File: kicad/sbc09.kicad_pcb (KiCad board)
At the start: 4 copper layers, 160 x 99.1 mm, 72 parts, among them J1 Conn_01x03_Male, J2 Conn_01x06_Male, J3 Conn_01x06_Male, J4 Conn_01x06_Male, J5 DB9_Female_MountingHoles, J6 Conn_02x25_Odd_Even, Q1 2N7000, SW1 SW_Push, U1 74LS245, U10 74LS670, U11 74LS670, U12 AS6C4008-55PCN, U13 SST39SF040-DIP, U14 SST39SF040-DIP, U15 XR68C681CJ, U16 MAX232, U2 74LS245, U3 74LS245, U4 ATF22V10C, U5 ATF22V10C, U6 MC6809E, U7 74HCT125, U8 74LS670, U9 74LS670, X1 8MHz, X2 3.6864MHz

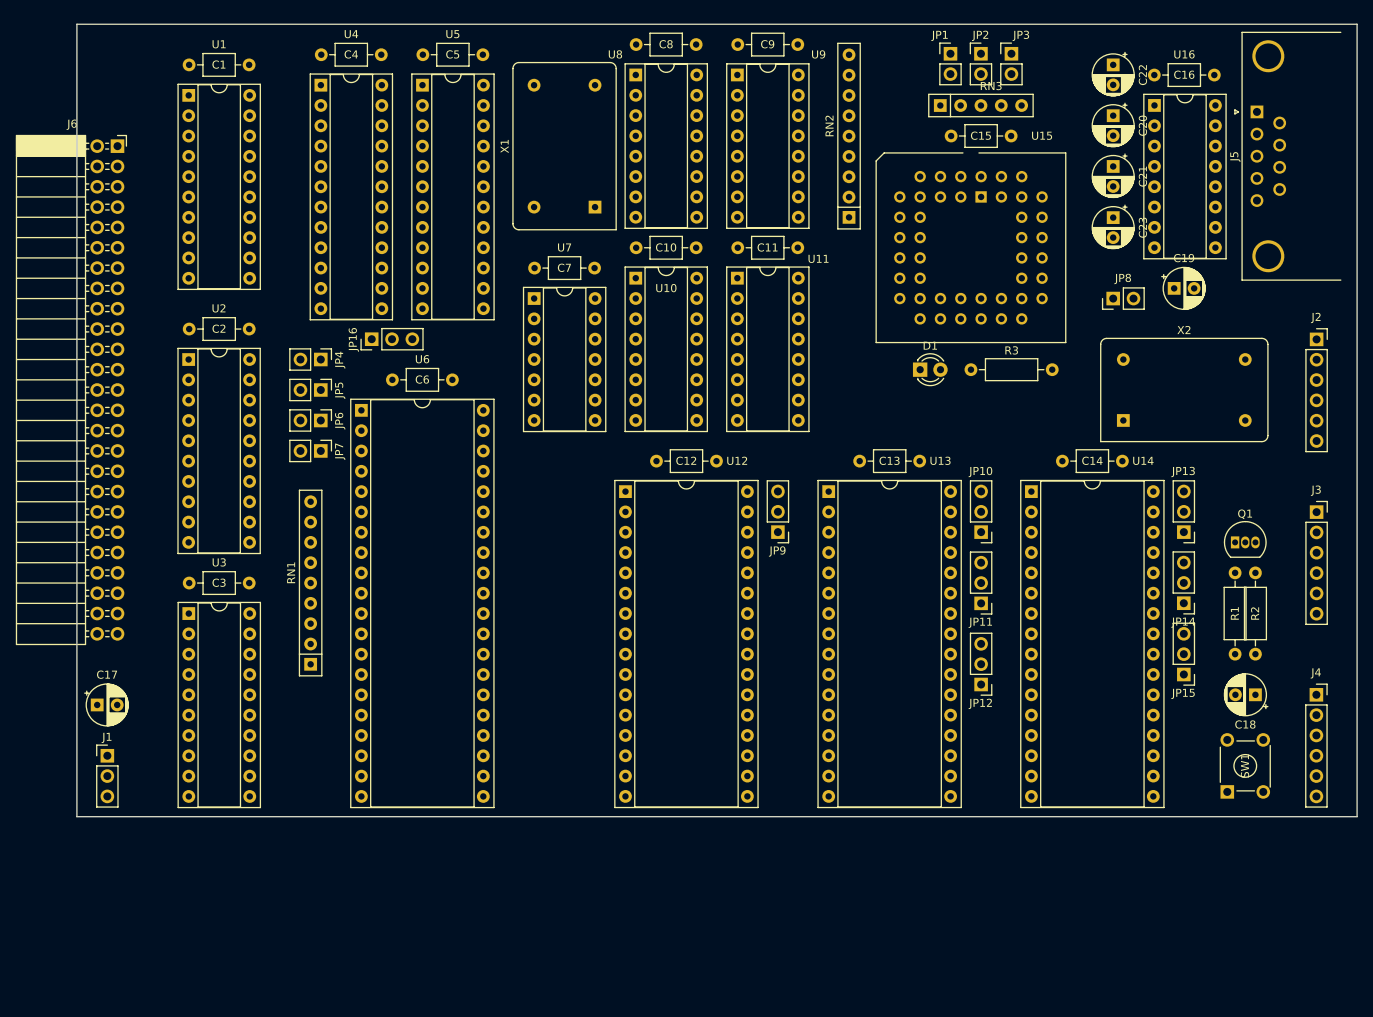
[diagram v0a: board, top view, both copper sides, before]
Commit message: Started manually routing the board
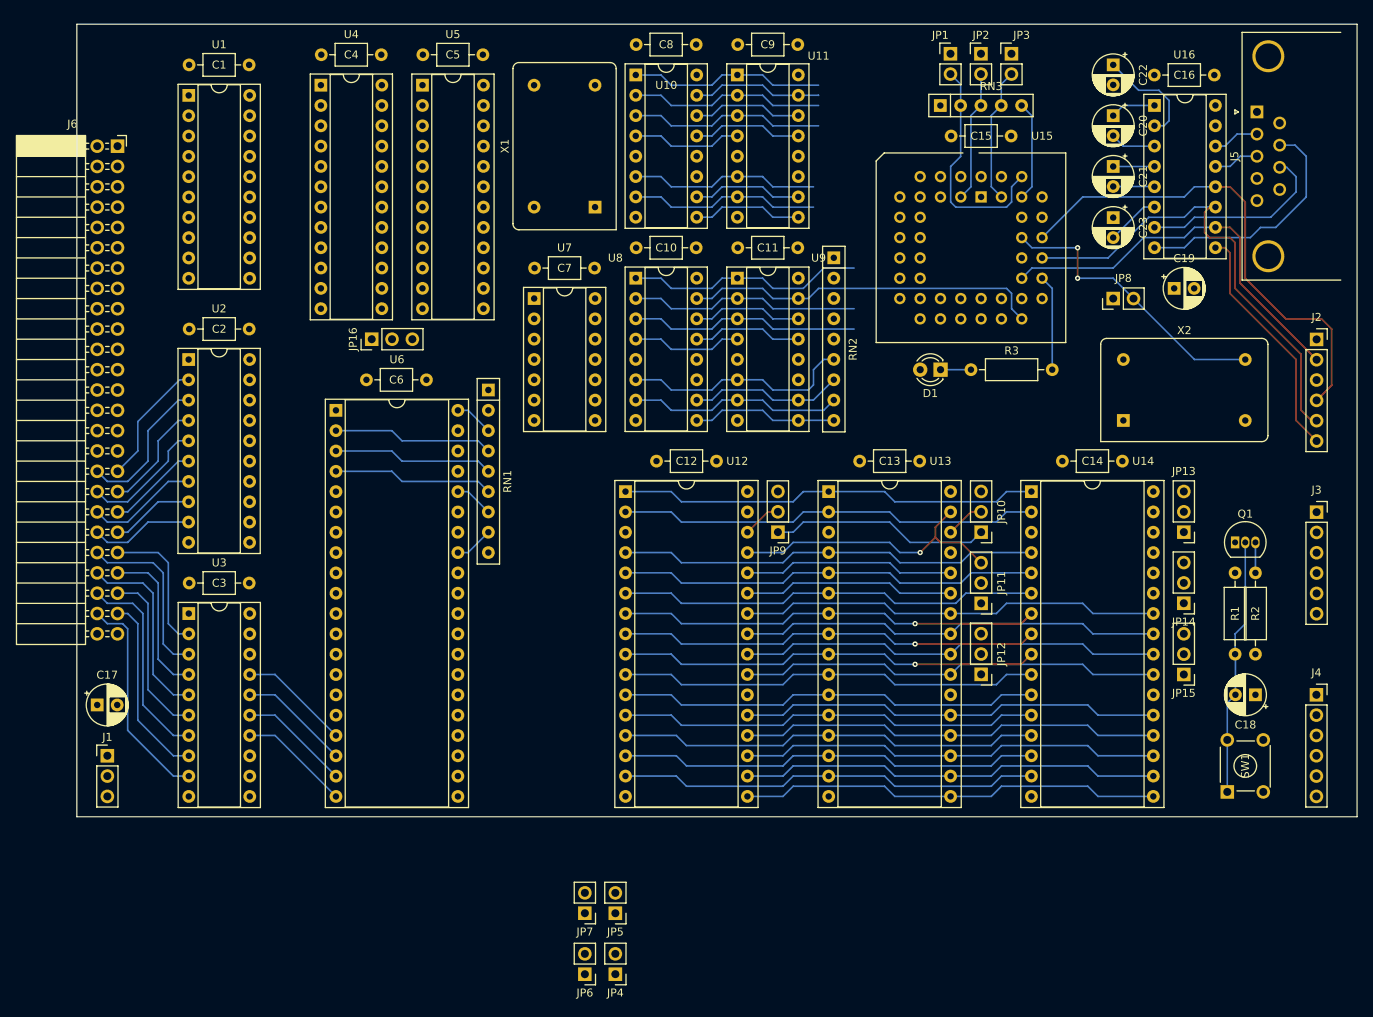
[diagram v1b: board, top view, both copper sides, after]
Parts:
- moved JP4 85.2 mm to (146.1, 169.5), turned to 180 degrees
- moved JP6 76.7 mm to (142.2, 169.5), turned to 180 degrees
- moved JP5 75.1 mm to (146.1, 161.9), turned to 180 degrees
- moved JP7 66.5 mm to (142.2, 161.9), turned to 180 degrees
- moved RN1 40.9 mm to (130.2, 96.5), turned to -90 degrees
- moved U10 25.4 mm to (148.6, 57.1)
- moved U11 25.4 mm to (161.3, 57.1)
- moved U8 25.4 mm to (148.6, 82.5)
- moved U9 25.4 mm to (161.3, 82.5)
- moved RN2 5.40 mm to (173.4, 80.0), turned to -90 degrees
- moved C6 3.25 mm to (114.9, 95.2)
- moved U6 3.18 mm to (111.1, 99.1)
- moved D1 2.54 mm to (186.7, 94.0), turned to 180 degrees
- moved JP12 1.27 mm to (191.8, 132.1)
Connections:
- JP5 pad 2: Net-(JP5-Pad2) -> Net-(RN1-Pad2)
- RN1 pad 2: nNMI -> Net-(RN1-Pad2)
- RN1 pad 3: nIRQ -> nHALT
- RN1 pad 4: nFIRQ -> nNMI
- RN1 pad 5: nHALT -> nIRQ
- RN1 pad 6: BUSY_BREQ -> nFIRQ
- RN1 pad 8: Net-(JP5-Pad2) -> BUSY_BREQ
- RN2 pad 7: /QA16 -> /QA14
- RN2 pad 8: /QA15 -> /QA16
- RN2 pad 9: /QA14 -> /QA15
- U7 pad 1: Net-(JP5-Pad2) -> Net-(RN1-Pad2)
- U7 pad 4: Net-(JP5-Pad2) -> Net-(RN1-Pad2)
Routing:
- net /D0: track 0.00 -> 97.7 mm
- net /D1: track 0.00 -> 82.8 mm
- net /D2: track 0.00 -> 81.7 mm
- net /D3: track 0.00 -> 81.7 mm
- net /A0: track 0.00 -> 80.3 mm
- net /A1: track 0.00 -> 80.3 mm
- net /QA16: track 0.00 -> 79.7 mm
- net /D7: track 0.00 -> 77.3 mm
- net /D5: track 0.00 -> 77.3 mm
- net /D6: track 0.00 -> 77.3 mm
- net /D4: track 0.00 -> 69.1 mm
- net /A10: track 0.00 -> 66.8 mm
- net /A12: track 0.00 -> 66.8 mm
- net /A9: track 0.00 -> 66.8 mm
- net /A11: track 0.00 -> 66.8 mm
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- added copper zone on In2.Cu, net VCC
- removed copper zone on In2.Cu, net (none)

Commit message: Started manually routing the board
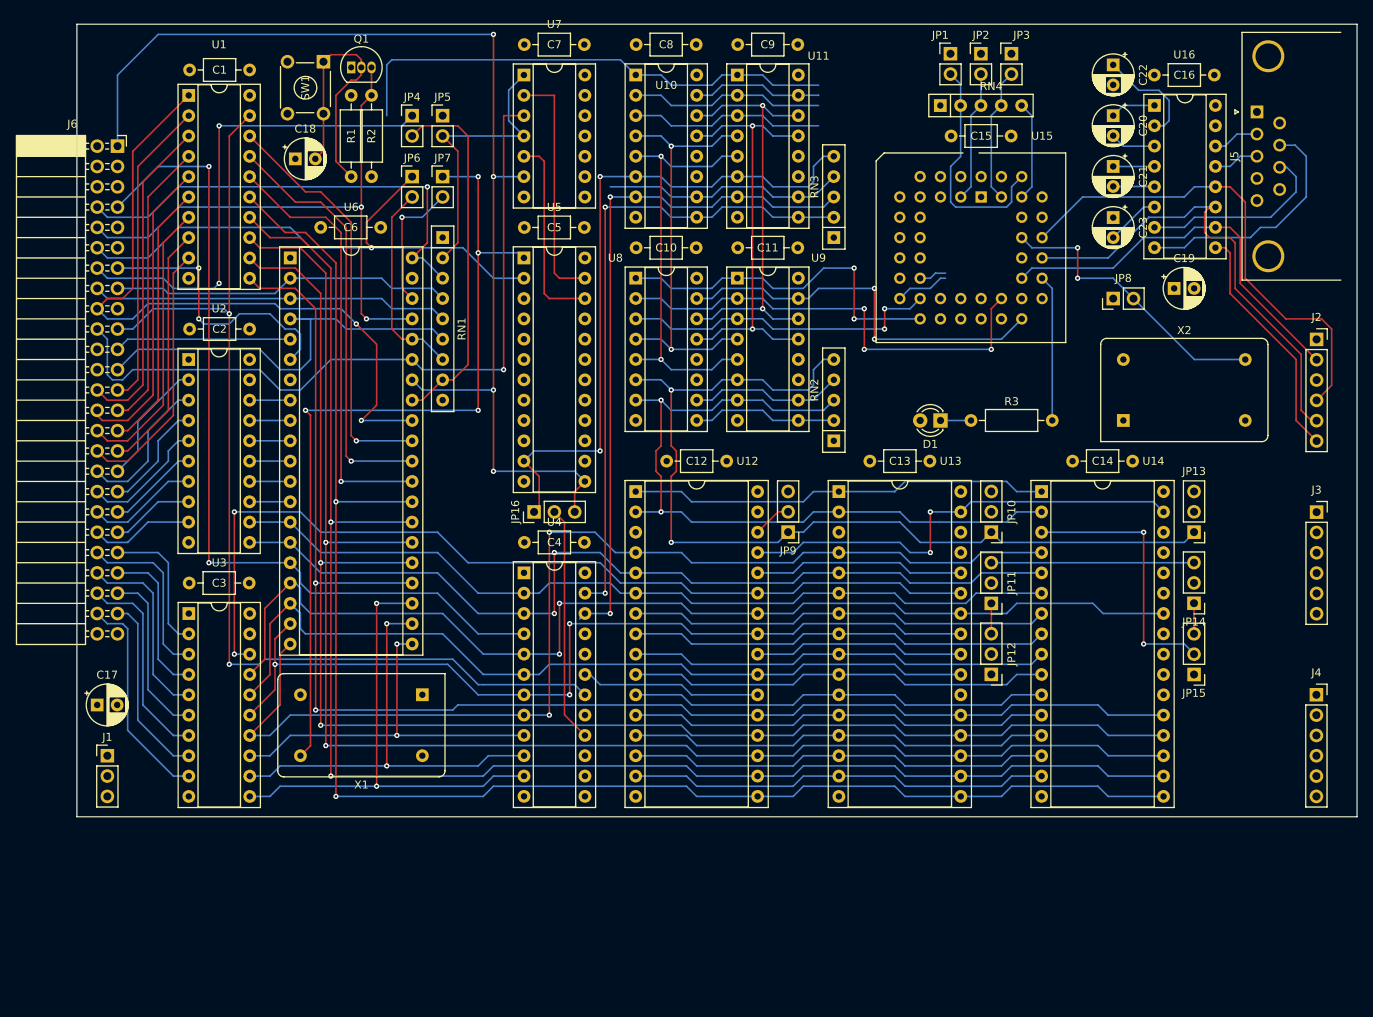
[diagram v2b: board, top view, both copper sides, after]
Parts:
- added RN3: 10K, Resistor_THT:R_Array_SIP5, F.Cu at (173.4, 77.5)
- RN2: footprint Resistor_THT:R_Array_SIP9 -> Resistor_THT:R_Array_SIP5
- moved SW1 145.2 mm to (109.6, 55.5), turned to -90 degrees
- moved C18 137.4 mm to (106.0, 67.6), turned to 0 degrees
- moved R1 125.6 mm to (113.0, 69.8)
- moved R2 125.6 mm to (115.6, 69.8)
- moved Q1 125.4 mm to (113.0, 56.2)
- moved JP4 110.3 mm to (120.7, 62.2), turned to 0 degrees
- moved JP5 102.0 mm to (124.5, 62.2), turned to 0 degrees
- moved JP6 102.0 mm to (120.7, 69.8), turned to 0 degrees
- moved JP7 93.8 mm to (124.5, 69.8), turned to 0 degrees
- moved U4 66.0 mm to (134.6, 119.4)
- moved C4 66.0 mm to (134.7, 115.6)
- moved X1 64.7 mm to (121.9, 134.6), turned to 180 degrees
- moved JP16 29.6 mm to (135.9, 111.8)
- moved C7 28.0 mm to (134.7, 53.3)
- moved U7 28.0 mm to (134.6, 57.1)
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- renumbered RN3 to RN4
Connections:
- RN2 pad 2: QA21 -> /QA15
- RN2 pad 3: QA20 -> /QA16
- RN2 pad 4: QA19 -> /QA14
- RN2 pad 5: /QA18 -> /QA17
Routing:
- net /D5: track 77.3 -> 251.5 mm, vias 0 -> 2
- net /D3: track 81.7 -> 237.2 mm, vias 0 -> 4
- net E: track 0.00 -> 143.4 mm, vias 0 -> 4
- net /D4: track 69.1 -> 210.0 mm, vias 0 -> 3
- net nCSEXT: track 0.00 -> 131.5 mm, vias 0 -> 2
- net /D6: track 77.3 -> 208.5 mm, vias 0 -> 2
- net /D7: track 77.3 -> 205.4 mm, vias 0 -> 2
- net /A14: track 0.00 -> 109.2 mm, vias 0 -> 4
- net A8: track 0.00 -> 106.9 mm, vias 0 -> 2
- net CLKX4: track 0.00 -> 105.2 mm, vias 0 -> 4
- net Q: track 0.00 -> 94.0 mm, vias 0 -> 1
- net /A8X: track 26.5 -> 115.8 mm, vias 0 -> 2
- net /A15: track 27.5 -> 115.6 mm, vias 0 -> 4
- net RnW: track 0.00 -> 87.5 mm, vias 0 -> 2
- net /D2: track 81.7 -> 165.1 mm, vias 0 -> 4
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
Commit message: Started manually routing the board
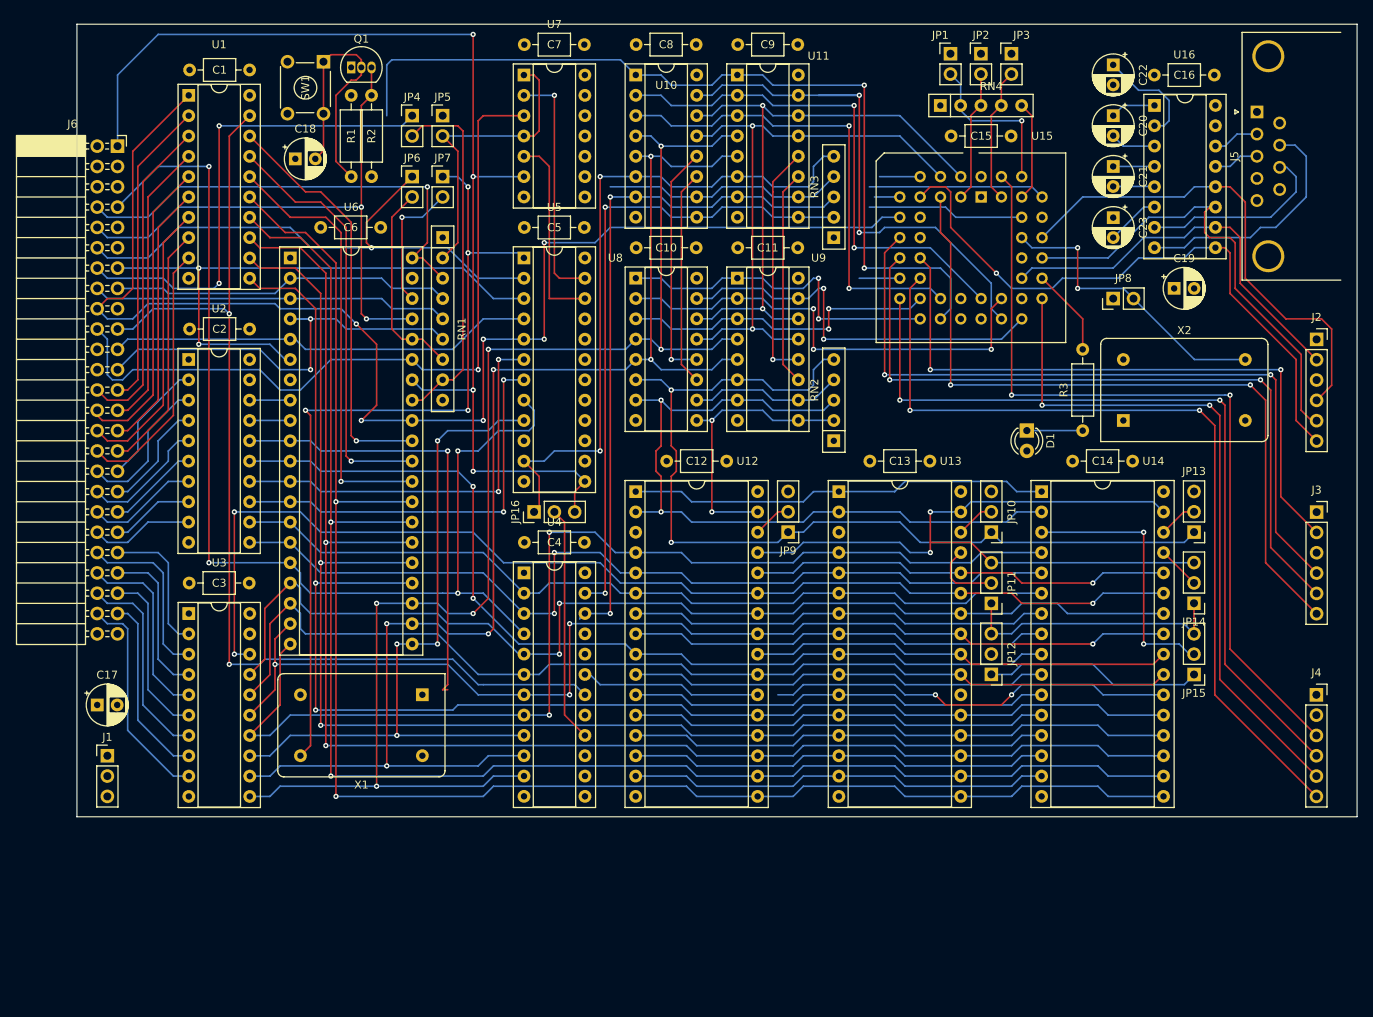
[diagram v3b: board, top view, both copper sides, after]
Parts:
- moved R3 14.0 mm to (204.5, 101.6), turned to 90 degrees
- moved D1 10.9 mm to (197.5, 101.6), turned to -90 degrees
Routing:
- net /SDCS: track 3.44 -> 107.5 mm, vias 0 -> 2
- net /SDMISO: track 0.00 -> 102.2 mm, vias 0 -> 2
- net /SDMOSI: track 6.77 -> 102.2 mm, vias 0 -> 2
- net /CTSB: track 0.00 -> 93.5 mm, vias 0 -> 2
- net /RXDB: track 0.00 -> 93.4 mm, vias 0 -> 2
- net /TXDB: track 0.00 -> 91.7 mm, vias 0 -> 2
- net /SDCLK: track 0.00 -> 86.2 mm, vias 0 -> 2
- net RnW: track 87.5 -> 172.0 mm, vias 2 -> 6
- net /RTSB: track 0.00 -> 80.5 mm, vias 0 -> 2
- net /A3: track 57.9 -> 122.5 mm, vias 0 -> 2
- net /A14: track 109.2 -> 170.9 mm, vias 4 -> 6
- net /A15: track 115.6 -> 176.5 mm, vias 4 -> 6
- net /A2: track 57.9 -> 114.0 mm, vias 0 -> 1
- net /D4: track 210.0 -> 261.9 mm, vias 3 -> 5
- net nCSROM1: track 0.00 -> 51.4 mm, vias 0 -> 2
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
